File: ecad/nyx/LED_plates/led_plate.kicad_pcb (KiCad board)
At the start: 2 copper layers, 110 x 35 mm, 13 parts, among them J1 JST SH 4

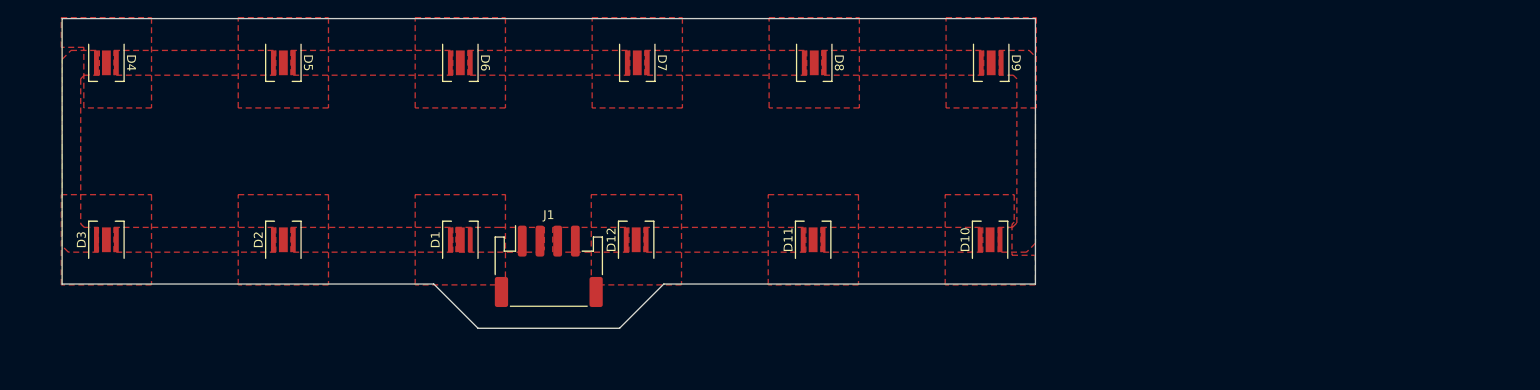
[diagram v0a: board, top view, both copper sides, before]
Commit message: Layouts a 2x6mm leds
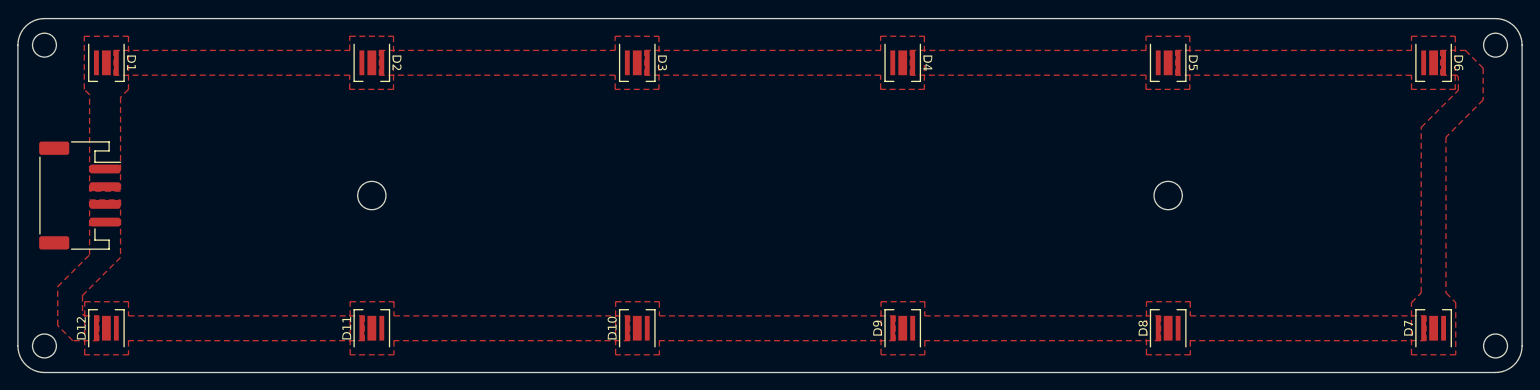
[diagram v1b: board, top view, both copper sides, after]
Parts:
- added REF**: MountingHole_3.2mm_M3, MountingHole:MountingHole_3.2mm_M3, F.Cu at (220.0, 115.0)
- added REF**: MountingHole_2.7mm_M2.5, MountingHole:MountingHole_2.7mm_M2.5, F.Cu at (257.0, 132.0)
- added REF**: MountingHole_2.7mm_M2.5, MountingHole:MountingHole_2.7mm_M2.5, F.Cu at (93.0, 98.0)
- added REF**: MountingHole_3.2mm_M3, MountingHole:MountingHole_3.2mm_M3, F.Cu at (130.0, 115.0)
- added REF**: MountingHole_2.7mm_M2.5, MountingHole:MountingHole_2.7mm_M2.5, F.Cu at (257.0, 98.0)
- added REF**: MountingHole_2.7mm_M2.5, MountingHole:MountingHole_2.7mm_M2.5, F.Cu at (93.0, 132.0)
- moved D6 110.0 mm to (250.0, 100.0)
- moved D5 100.0 mm to (220.0, 100.0)
- moved D7 94.9 mm to (250.0, 130.0), turned to 90 degrees
- moved D4 90.0 mm to (190.0, 100.0)
- moved D3 63.2 mm to (160.0, 100.0), turned to -90 degrees
- moved D12 60.7 mm to (100.0, 130.0)
- moved J1 53.6 mm to (97.0, 115.0), turned to -90 degrees
- moved D11 50.9 mm to (130.0, 130.0)
- moved D8 50.0 mm to (220.0, 130.0), turned to 90 degrees
- moved D1 44.7 mm to (100.0, 100.0), turned to -90 degrees
- moved D10 41.1 mm to (160.0, 130.0)
- moved D9 31.6 mm to (190.0, 130.0), turned to 90 degrees
- moved D2 22.4 mm to (130.0, 100.0), turned to -90 degrees
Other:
- board size 110 x 35 mm -> 170 x 40 mm
